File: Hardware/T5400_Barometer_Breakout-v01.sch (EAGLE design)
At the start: 11 parts, among them U1 T5400

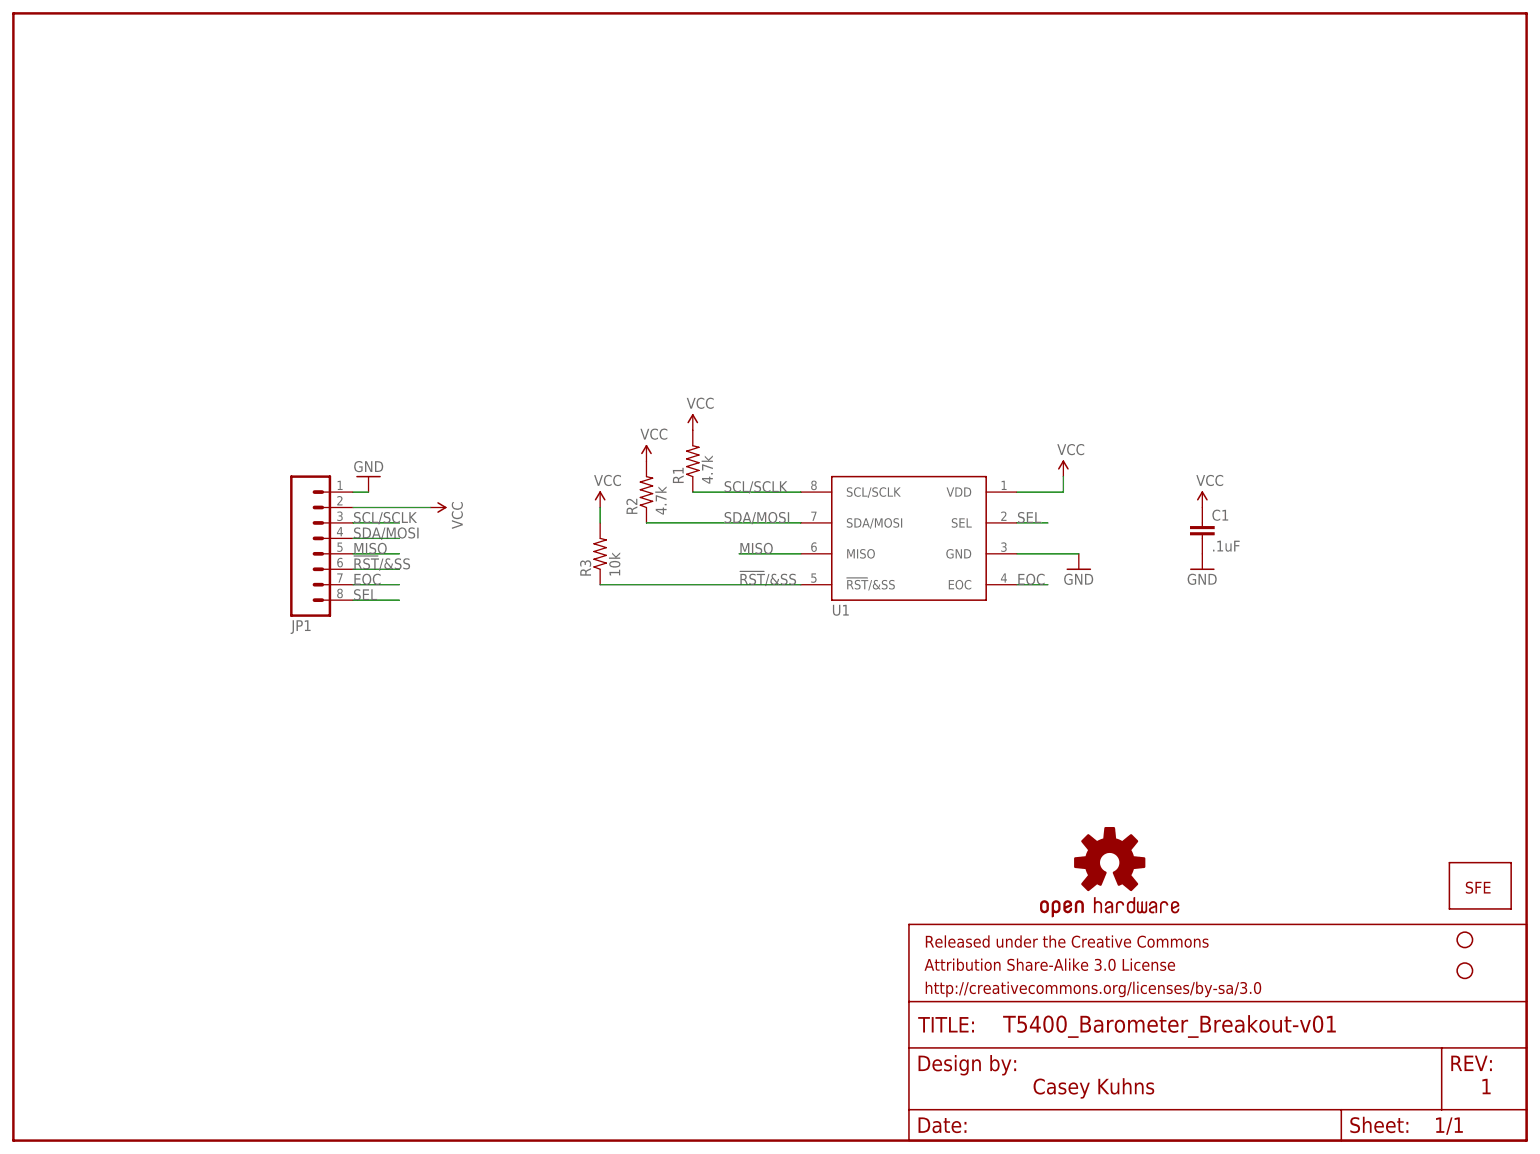
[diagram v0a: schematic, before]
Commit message: corrected file names to reflect PROTO status made minor modifications to apperance
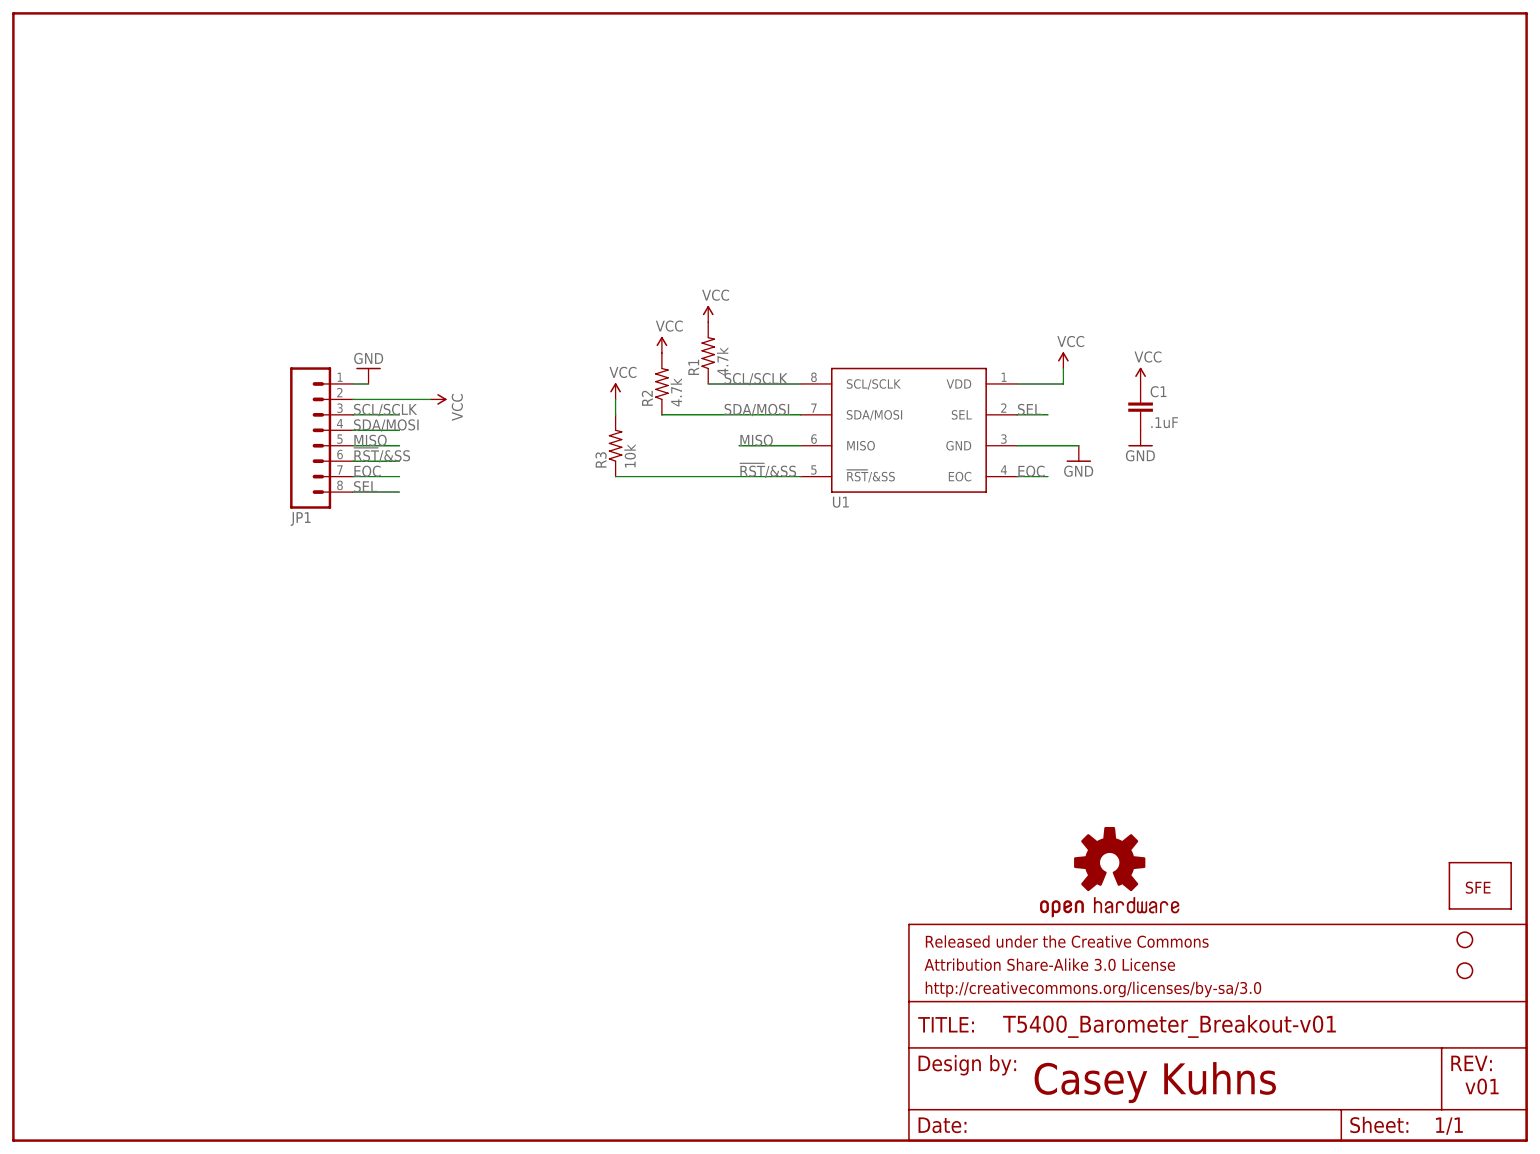
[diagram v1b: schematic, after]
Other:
- note added: "v01"
- note removed: "1"
- moved on the sheet: C1, JP1, R1, R2, R3, U1
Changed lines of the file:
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@@
 <sheet>
 <plain>
-<text x="167.64" y="7.62" size="2.54" layer="94">Casey Kuhns</text>
-<text x="241.3" y="7.62" size="2.54" layer="94">1</text>
+<text x="167.64" y="7.62" size="5.08" layer="94" font="vector">Casey Kuhns</text>
+<text x="238.76" y="7.62" size="2.54" layer="94" font="vector">v01</text>
 </plain>
 <instances>
-<instance part="U1" gate="U$1" x="147.32" y="99.06"/>
-<instance part="JP1" gate="G$1" x="50.8" y="99.06" rot="MR180"/>
-<instance part="GND1" gate="1" x="175.26" y="93.98"/>
+<instance part="U1" gate="U$1" x="147.32" y="116.84"/>
+<instance part="JP1" gate="G$1" x="50.8" y="116.84" rot="MR180"/>
+<instance part="GND1" gate="1" x="175.26" y="111.76"/>
 <instance part="FRAME1" gate="G$1" x="0" y="0"/>
 <instance part="FRAME1" gate="G$2" x="147.32" y="0"/>
 <instance part="LOGO2" gate="G$1" x="180.34" y="45.72"/>
-<instance part="R1" gate="G$1" x="111.76" y="111.76" rot="R90"/>
-<instance part="R2" gate="G$1" x="104.14" y="106.68" rot="R90"/>
-<instance part="SUPPLY1" gate="1" x="172.72" y="109.22"/>
-<instance part="SUPPLY2" gate="1" x="111.76" y="116.84"/>
-<instance part="SUPPLY3" gate="1" x="104.14" y="111.76"/>
-<instance part="C1" gate="G$1" x="195.58" y="99.06"/>
-<instance part="SUPPLY5" gate="1" x="195.58" y="104.14"/>
-<instance part="GND3" gate="1" x="195.58" y="93.98"/>
-<instance part="SUPPLY4" gate="1" x="68.58" y="104.14" rot="R270"/>
-<instance part="GND2" gate="1" x="58.42" y="109.22" rot="R180"/>
+<instance part="R1" gate="G$1" x="114.3" y="129.54" rot="R90"/>
+<instance part="R2" gate="G$1" x="106.68" y="124.46" rot="R90"/>
+<instance part="SUPPLY1" gate="1" x="172.72" y="127"/>
+<instance part="SUPPLY2" gate="1" x="114.3" y="134.62"/>
+<instance part="SUPPLY3" gate="1" x="106.68" y="129.54"/>
+<instance part="C1" gate="G$1" x="185.42" y="119.38"/>
+<instance part="SUPPLY5" gate="1" x="185.42" y="124.46"/>
+<instance part="GND3" gate="1" x="185.42" y="114.3"/>
+<instance part="SUPPLY4" gate="1" x="68.58" y="121.92" rot="R270"/>
+<instance part="GND2" gate="1" x="58.42" y="127" rot="R180"/>
 <instance part="STANDOFF1" gate="G$1" x="238.76" y="27.94"/>
 <instance part="STANDOFF2" gate="G$1" x="238.76" y="33.02"/>
 <instance part="LOGO1" gate="G$1" x="238.76" y="40.64"/>
-<instance part="R3" gate="G$1" x="96.52" y="96.52" rot="R90"/>
-<instance part="SUPPLY6" gate="1" x="96.52" y="104.14"/>
+<instance part="R3" gate="G$1" x="99.06" y="114.3" rot="R90"/>
+<instance part="SUPPLY6" gate="1" x="99.06" y="121.92"/>
 </instances>
 <busses>
@@
 <pinref part="U1" gate="U$1" pin="GND"/>
 <pinref part="GND1" gate="1" pin="GND"/>
-<wire x1="175.26" y1="96.52" x2="165.1" y2="96.52" width="0.1524" layer="91"/>
+<wire x1="175.26" y1="114.3" x2="165.1" y2="114.3" width="0.1524" layer="91"/>
 </segment>
 <segment>
@@
 <segment>
 <pinref part="JP1" gate="G$1" pin="1"/>
-<wire x1="55.88" y1="106.68" x2="58.42" y2="106.68" width="0.1524" layer="91"/>
+<wire x1="55.88" y1="124.46" x2="58.42" y2="124.46" width="0.1524" layer="91"/>
 <pinref part="GND2" gate="1" pin="GND"/>
 </segment>
@@
 <segment>
 <pinref part="U1" gate="U$1" pin="SEL"/>
-<wire x1="165.1" y1="101.6" x2="170.18" y2="101.6" width="0.1524" layer="91"/>
-<label x="165.1" y="101.6" size="1.778" layer="95"/>
+<wire x1="165.1" y1="119.38" x2="170.18" y2="119.38" width="0.1524" layer="91"/>
+<label x="165.1" y="119.38" size="1.778" layer="95"/>
 </segment>
 <segment>
 <pinref part="JP1" gate="G$1" pin="8"/>
-<wire x1="55.88" y1="88.9" x2="63.5" y2="88.9" width="0.1524" layer="91"/>
-<label x="55.88" y="88.9" size="1.778" layer="95"/>
+<wire x1="55.88" y1="106.68" x2="63.5" y2="106.68" width="0.1524" layer="91"/>
+<label x="55.88" y="106.68" size="1.778" layer="95"/>
 </segment>
 </net>
@@
 <segment>
 <pinref part="U1" gate="U$1" pin="EOC"/>
-<wire x1="165.1" y1="91.44" x2="170.18" y2="91.44" width="0.1524" layer="91"/>
-<label x="165.1" y="91.44" size="1.778" layer="95"/>
+<wire x1="165.1" y1="109.22" x2="170.18" y2="109.22" width="0.1524" layer="91"/>
+<label x="165.1" y="109.22" size="1.778" layer="95"/>
 </segment>
 <segment>
 <pinref part="JP1" gate="G$1" pin="7"/>
-<wire x1="55.88" y1="91.44" x2="63.5" y2="91.44" width="0.1524" layer="91"/>
-<label x="55.88" y="91.44" size="1.778" layer="95"/>
+<wire x1="55.88" y1="109.22" x2="63.5" y2="109.22" width="0.1524" layer="91"/>
+<label x="55.88" y="109.22" size="1.778" layer="95"/>
 </segment>
 </net>
@@
 <segment>
 <pinref part="U1" gate="U$1" pin="!RST!/&amp;SS"/>
-<wire x1="129.54" y1="91.44" x2="96.52" y2="91.44" width="0.1524" layer="91"/>
-<label x="119.38" y="91.44" size="1.778" layer="95"/>
+<wire x1="129.54" y1="109.22" x2="99.06" y2="109.22" width="0.1524" layer="91"/>
+<label x="119.38" y="109.22" size="1.778" layer="95"/>
 <pinref part="R3" gate="G$1" pin="1"/>
 </segment>
 <segment>
 <pinref part="JP1" gate="G$1" pin="6"/>
-<wire x1="55.88" y1="93.98" x2="63.5" y2="93.98" width="0.1524" layer="91"/>
-<label x="55.88" y="93.98" size="1.778" layer="95"/>
+<wire x1="55.88" y1="111.76" x2="63.5" y2="111.76" width="0.1524" layer="91"/>
+<label x="55.88" y="111.76" size="1.778" layer="95"/>
 </segment>
 </net>
@@
 <segment>
 <pinref part="U1" gate="U$1" pin="MISO"/>
-<wire x1="129.54" y1="96.52" x2="119.38" y2="96.52" width="0.1524" layer="91"/>
-<label x="119.38" y="96.52" size="1.778" layer="95"/>
+<wire x1="129.54" y1="114.3" x2="119.38" y2="114.3" width="0.1524" layer="91"/>
+<label x="119.38" y="114.3" size="1.778" layer="95"/>
 </segment>
 <segment>
 <pinref part="JP1" gate="G$1" pin="5"/>
-<wire x1="55.88" y1="96.52" x2="63.5" y2="96.52" width="0.1524" layer="91"/>
-<label x="55.88" y="96.52" size="1.778" layer="95"/>
+<wire x1="55.88" y1="114.3" x2="63.5" y2="114.3" width="0.1524" layer="91"/>
+<label x="55.88" y="114.3" size="1.778" layer="95"/>
 </segment>
 </net>
@@
 <segment>
 <pinref part="U1" gate="U$1" pin="SDA/MOSI"/>
-<wire x1="129.54" y1="101.6" x2="104.14" y2="101.6" width="0.1524" layer="91"/>
+<wire x1="129.54" y1="119.38" x2="106.68" y2="119.38" width="0.1524" layer="91"/>
 <pinref part="R2" gate="G$1" pin="1"/>
-<label x="116.84" y="101.6" size="1.778" layer="95"/>
+<label x="116.84" y="119.38" size="1.778" layer="95"/>
 </segment>
 <segment>
 <pinref part="JP1" gate="G$1" pin="4"/>
-<wire x1="55.88" y1="99.06" x2="63.5" y2="99.06" width="0.1524" layer="91"/>
-<label x="55.88" y="99.06" size="1.778" layer="95"/>
+<wire x1="55.88" y1="116.84" x2="63.5" y2="116.84" width="0.1524" layer="91"/>
+<label x="55.88" y="116.84" size="1.778" layer="95"/>
 </segment>
 </net>
@@
 <segment>
 <pinref part="U1" gate="U$1" pin="SCL/SCLK"/>
-<wire x1="129.54" y1="106.68" x2="111.76" y2="106.68" width="0.1524" layer="91"/>
+<wire x1="129.54" y1="124.46" x2="114.3" y2="124.46" width="0.1524" layer="91"/>
 <pinref part="R1" gate="G$1" pin="1"/>
-<label x="116.84" y="106.68" size="1.778" layer="95"/>
+<label x="116.84" y="124.46" size="1.778" layer="95"/>
 </segment>
 <segment>
 <pinref part="JP1" gate="G$1" pin="3"/>
-<wire x1="55.88" y1="101.6" x2="63.5" y2="101.6" width="0.1524" layer="91"/>
-<label x="55.88" y="101.6" size="1.778" layer="95"/>
+<wire x1="55.88" y1="119.38" x2="63.5" y2="119.38" width="0.1524" layer="91"/>
+<label x="55.88" y="119.38" size="1.778" layer="95"/>
 </segment>
 </net>
@@
 <segment>
 <pinref part="U1" gate="U$1" pin="VDD"/>
-<wire x1="165.1" y1="106.68" x2="172.72" y2="106.68" width="0.1524" layer="91"/>
+<wire x1="165.1" y1="124.46" x2="172.72" y2="124.46" width="0.1524" layer="91"/>
 <pinref part="SUPPLY1" gate="1" pin="VCC"/>
-<wire x1="172.72" y1="106.68" x2="172.72" y2="109.22" width="0.1524" layer="91"/>
+<wire x1="172.72" y1="124.46" x2="172.72" y2="127" width="0.1524" layer="91"/>
 </segment>
 <segment>
@@
 <segment>
 <pinref part="JP1" gate="G$1" pin="2"/>
-<wire x1="68.58" y1="104.14" x2="55.88" y2="104.14" width="0.1524" layer="91"/>
+<wire x1="68.58" y1="121.92" x2="55.88" y2="121.92" width="0.1524" layer="91"/>
 <pinref part="SUPPLY4" gate="1" pin="VCC"/>
 </segment>
@@
 <pinref part="R3" gate="G$1" pin="2"/>
 <pinref part="SUPPLY6" gate="1" pin="VCC"/>
-<wire x1="96.52" y1="104.14" x2="96.52" y2="101.6" width="0.1524" layer="91"/>
+<wire x1="99.06" y1="121.92" x2="99.06" y2="119.38" width="0.1524" layer="91"/>
 </segment>
 </net>
